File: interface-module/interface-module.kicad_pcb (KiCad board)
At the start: 2 copper layers, 79 x 83 mm, 113 parts, among them J1 Conn_01x08, J2 Conn_01x08, J3 Conn_01x02, Q201 DMP3050LVT-7, Q202 DMP3050LVT-7, Q203 DMP3050LVT-7, Q204 DMP3050LVT-7, Q205 DMP3050LVT-7, Q206 DMP3050LVT-7, Q207 DMP3050LVT-7, Q208 DMP3050LVT-7, SW1 SW_Coded_SH-7050, U101 MCP3464, U201 140357145200, U202 140357145200, U203 140357145200, U204 140357145200, U205 140357145200, U206 140357145200, U207 140357145200, U208 140357145200, U301 TCA9548

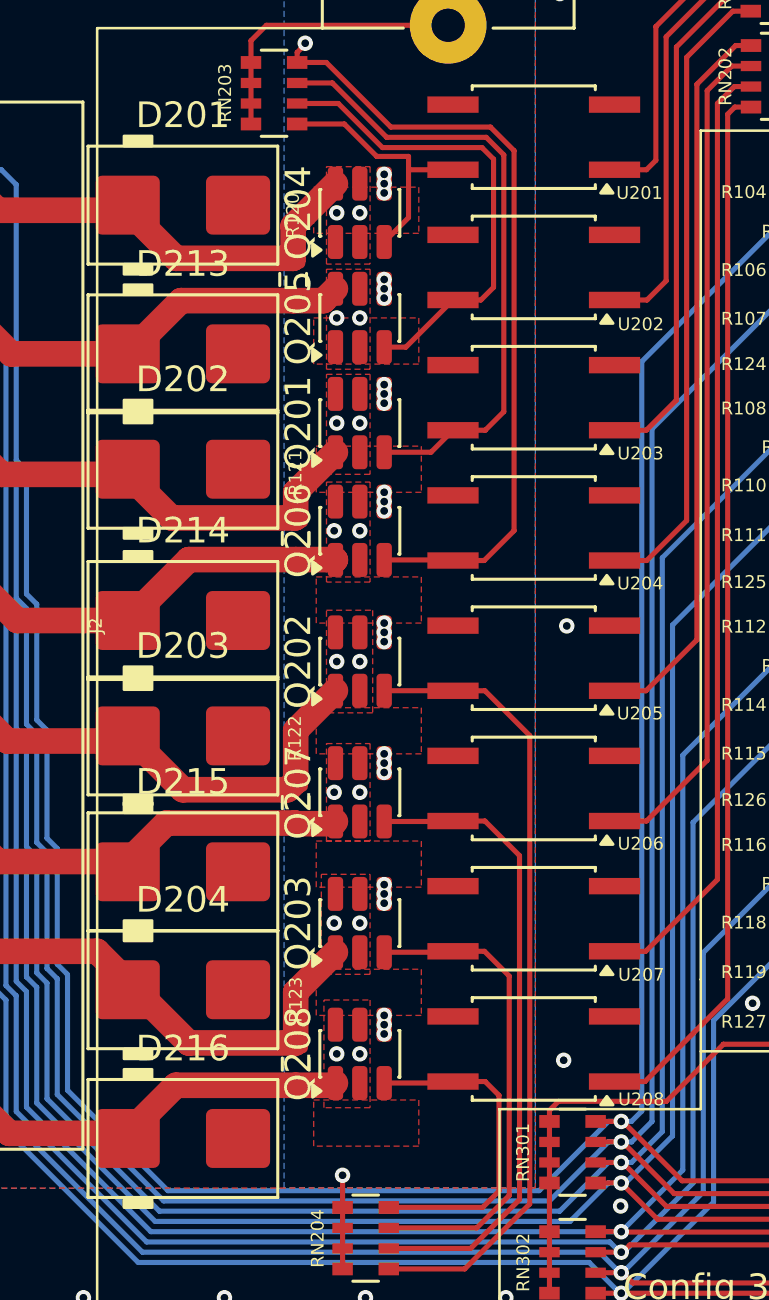
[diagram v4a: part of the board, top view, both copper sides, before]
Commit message: Better vpow contact
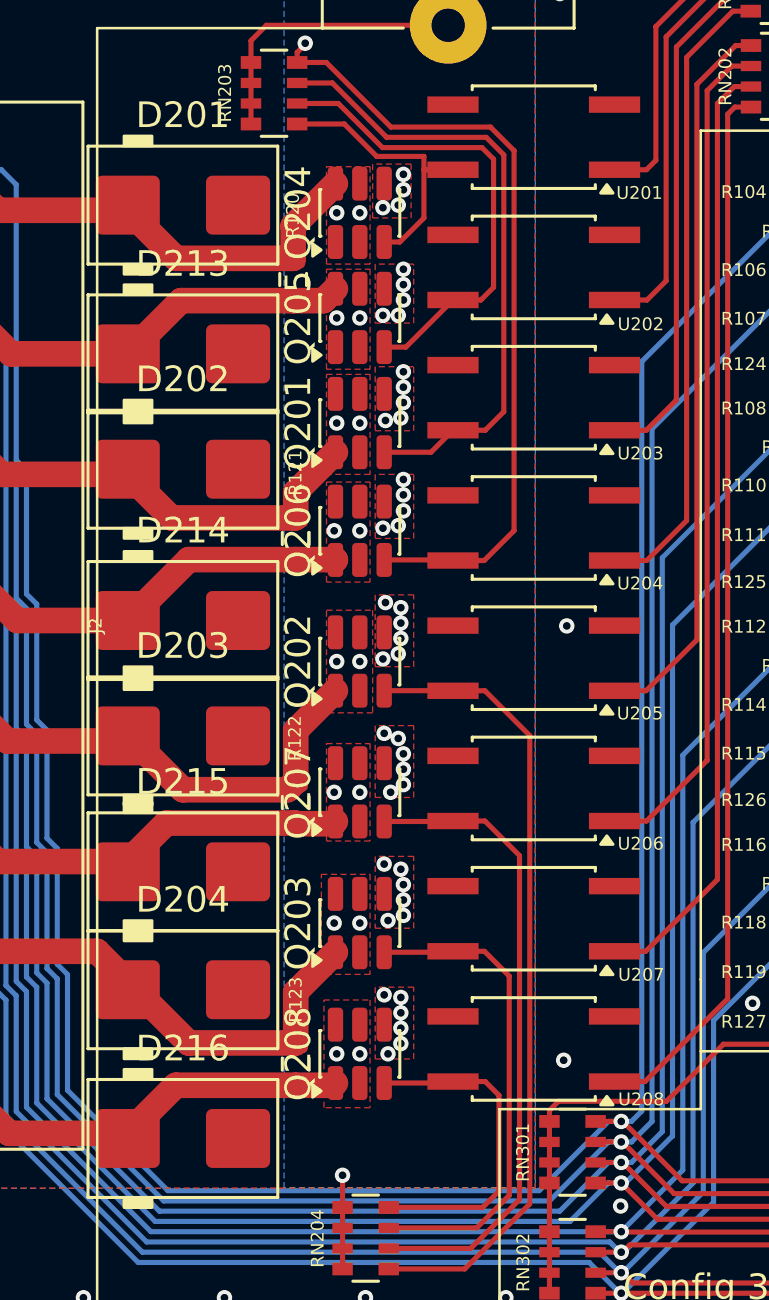
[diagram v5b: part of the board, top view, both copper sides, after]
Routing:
- net /outputs/~{ISO_OUT_0}: track 10.3 -> 10.9 mm
- net VPOW: vias 25 -> 44

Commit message: Ready for more scrutiny
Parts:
- R120, R121, R122, R123: moved to B.Cu
- moved R123 16.4 mm to (109.8, 130.2)
- moved R122 16.4 mm to (109.8, 120.1)
- moved R121 16.4 mm to (109.8, 109.9)
- moved R120 16.3 mm to (109.8, 99.8)
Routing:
- net OUT5/IN2-: track 98.1 -> 102.2 mm, vias 4 -> 2
- net OUT7/IN3-: track 84.9 -> 88.8 mm, vias 4 -> 2
- net OUT3/IN1-: track 114.9 -> 118.5 mm, vias 4 -> 2
- net OUT1/IN0-: track 131.4 -> 135.0 mm, vias 4 -> 2
- net OUT2/IN1+: track 122.2 -> 125.3 mm, vias 4 -> 2
- net OUT0/IN0+: track 140.1 -> 142.7 mm, vias 4 -> 2
- net OUT6/IN3+: track 92.3 -> 93.9 mm, vias 4 -> 2
- net OUT4/IN2+: track 106.9 -> 108.3 mm, vias 4 -> 2
- net GND: vias 32 -> 48

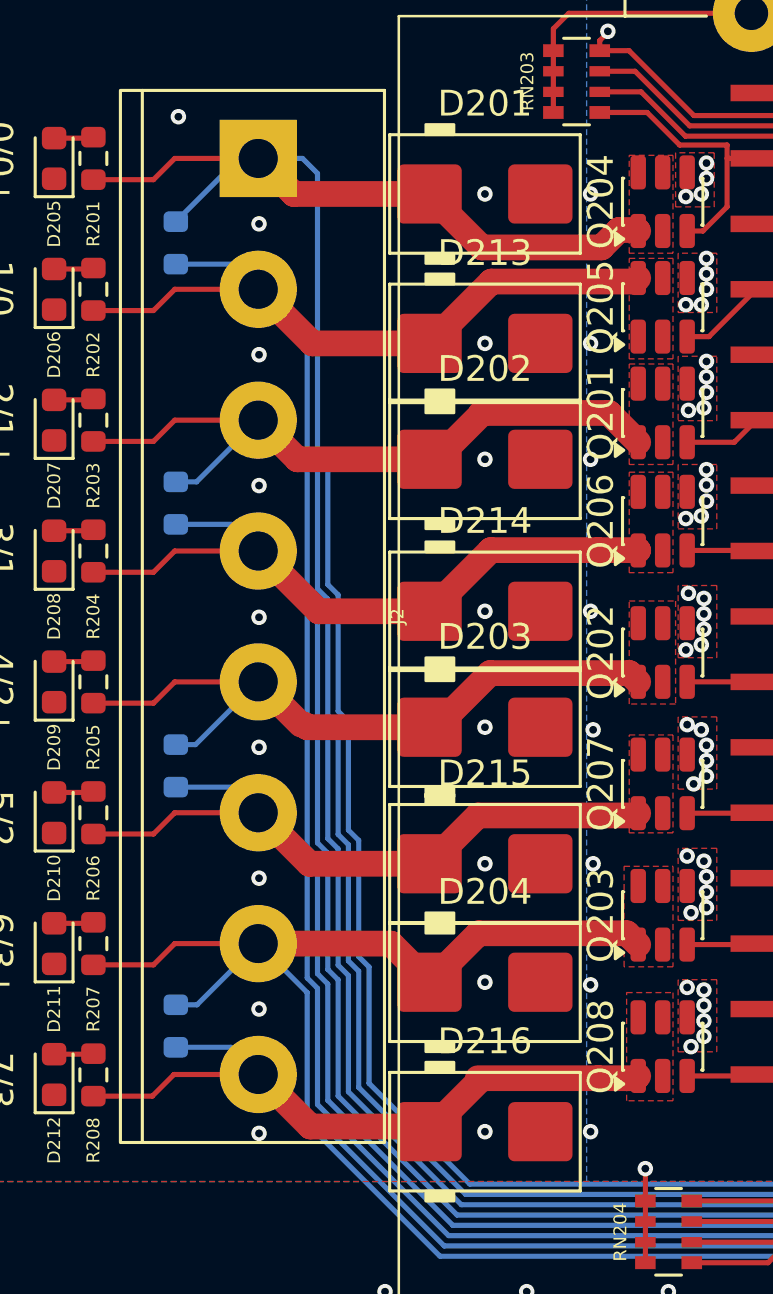
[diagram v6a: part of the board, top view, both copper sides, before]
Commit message: Better via placement and updated filled zones
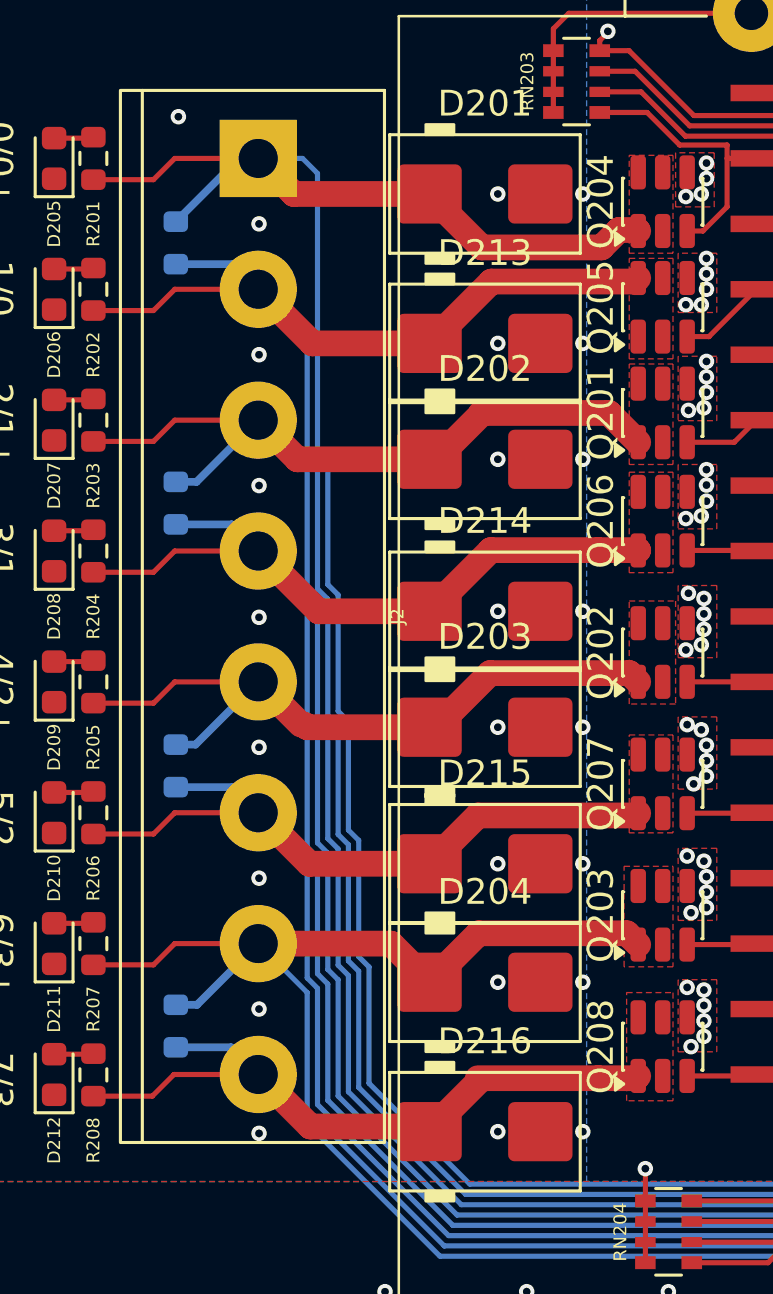
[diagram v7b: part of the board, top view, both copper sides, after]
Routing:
- net GND: vias 48 -> 32
- net AUX_POW-: vias 21 -> 37

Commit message: Upgraded to v1.1.
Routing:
- net /outputs/~{ISO_OUT_3}: track 31.1 -> 30.3 mm
- net AUX_POW-: vias 37 -> 36
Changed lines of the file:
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@@
 	(title_block
 		(title "minTS Interface Module")
-		(date "2024-05-05")
-		(rev "v1.0")
-		(company "PSAS")
+		(date "2025-12-23")
+		(rev "v1.1")
+		(company "Portland State Aerospace Society")
 	)
 	(layers
@@
 	)
 	(via
-		(at 126.571 91.585999)
-		(size 0.6)
-		(drill 0.3)
-		(layers "F.Cu" "B.Cu")
-		(free yes)
-		(net 89)
-	)
-	(via
 		(at 125.6 123.9)
 		(size 0.6)
@@
 	)
 	(segment
-		(start 126.256 92.336001)
-		(end 126.256 91.944)
-		(width 0.2)
-		(layer "F.Cu")
-		(net 106)
-	)
-	(segment
 		(start 133.796 94.856001)
 		(end 134.716 95.776001)
@@
 		(width 0.2)
 		(layer "F.Cu")
-		(net 106)
-	)
-	(segment
-		(start 126.256 91.944)
-		(end 126.6 91.6)
-		(width 0.2)
-		(layer "F.Cu")
